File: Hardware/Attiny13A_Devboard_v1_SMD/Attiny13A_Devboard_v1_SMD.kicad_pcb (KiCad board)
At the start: 2 copper layers, 0 parts

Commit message: Attiny13A Dev Board SMD - Layout - Initial Placement done
Signed-off-by: alexanderjg85 <alexanderjg85@gmail.com>
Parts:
- added C1: 10 uF, Capacitor_SMD:C_1206_3216Metric_Pad1.33x1.80mm_HandSolder, F.Cu at (138.8, 64.2)
- added C2: 100 nF, Capacitor_SMD:C_1206_3216Metric_Pad1.33x1.80mm_HandSolder, F.Cu at (156.2, 80.5)
- added D1: SS14, Diode_SMD:D_SMA_Handsoldering, F.Cu at (130.5, 62.8)
- added D2: RED, LED_SMD:LED_1206_3216Metric_Pad1.42x1.75mm_HandSolder, F.Cu at (139.8, 79.2)
- added J1: Screw_Terminal_01x02, TerminalBlock_Phoenix:TerminalBlock_Phoenix_MKDS-1,5-2-5.08_1x02_P5.08mm_Horizontal, F.Cu at (128.6, 71.2)
- added J2: AVR-ISP-6, Connector_PinHeader_2.54mm:PinHeader_2x03_P2.54mm_Vertical, F.Cu at (156.2, 62.4)
- added J3: Conn_01x06_Pin, Connector_PinHeader_2.54mm:PinHeader_1x06_P2.54mm_Vertical, F.Cu at (168.5, 79.3)
- added R1: 470, Resistor_SMD:R_1206_3216Metric_Pad1.30x1.75mm_HandSolder, F.Cu at (146.2, 79.2)
- added R2: 10k, Resistor_SMD:R_1206_3216Metric_Pad1.30x1.75mm_HandSolder, F.Cu at (148.5, 64.2)
- added SW1: SW_Push, Button_Switch_SMD:SW_SPST_PTS647_Sx38, F.Cu at (143.5, 71.2)
- added TP1: TP_5V, TestPoint:TestPoint_Pad_D1.5mm, F.Cu at (125.2, 66.5)
- added TP2: TP_AVRLED, TestPoint:TestPoint_Pad_D1.5mm, F.Cu at (149.2, 75.8)
- added TP3: TP_VCC, TestPoint:TestPoint_Pad_D1.5mm, F.Cu at (143.8, 62.5)
- added TP4: TP_AVR_RST, TestPoint:TestPoint_Pad_D1.5mm, F.Cu at (150.2, 69.2)
- added TP5: TP_AVR_PB3, TestPoint:TestPoint_Pad_D1.5mm, F.Cu at (162.5, 69.5)
- added TP6: TP_AVR_SCK, TestPoint:TestPoint_Pad_D1.5mm, F.Cu at (152.8, 65.0)
- added TP7: TP_AVR_MISO, TestPoint:TestPoint_Pad_D1.5mm, F.Cu at (162.8, 74.2)
- added TP8: TP_AVR_MOSI, TestPoint:TestPoint_Pad_D1.5mm, F.Cu at (162.8, 77.8)
- added TP9: TP_GND, TestPoint:TestPoint_Pad_D1.5mm, F.Cu at (128.8, 81.5)
- added U1: ATtiny13A-SS, Package_SO:SOIC-8_3.9x4.9mm_P1.27mm, F.Cu at (156.0, 75.0)
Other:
- board outline added: 48 x 24 mm

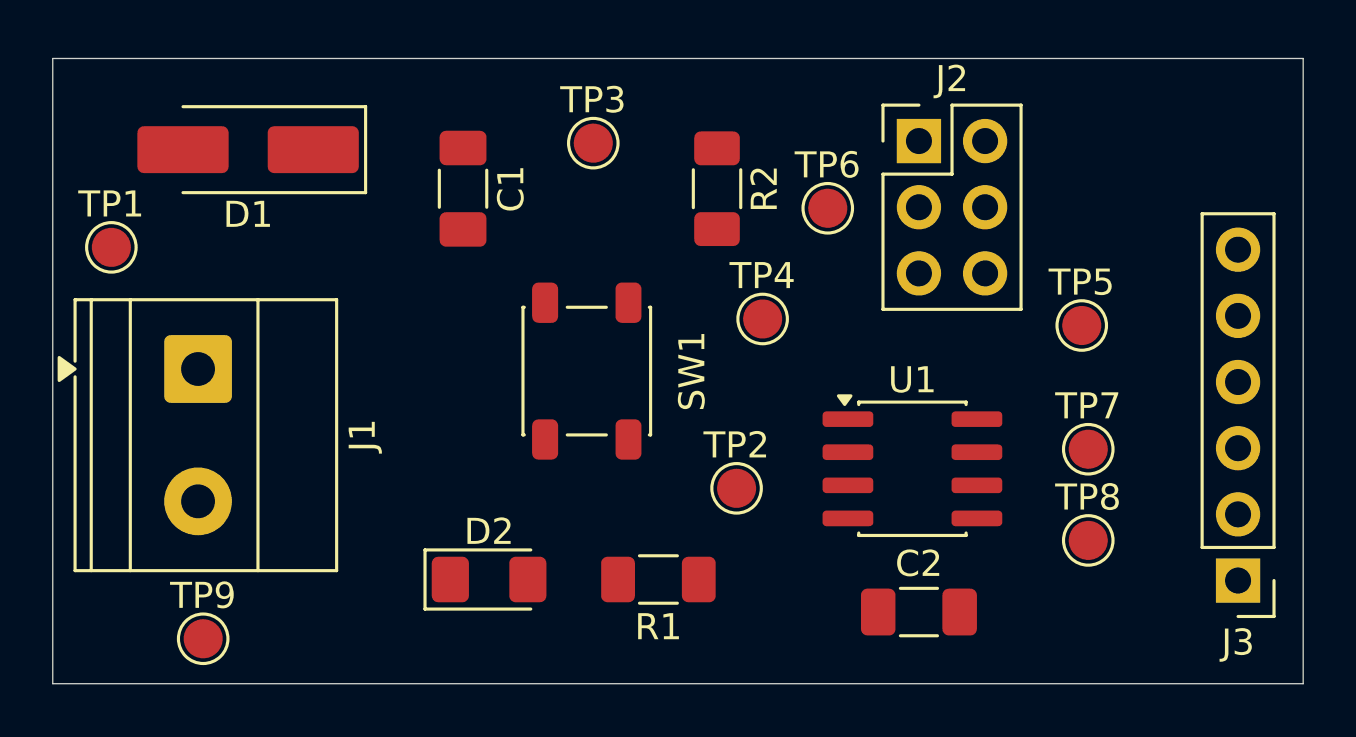
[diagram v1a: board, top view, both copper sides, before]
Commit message: Attiny13A Dev Board SMD - Layout - Initial Routing done
Signed-off-by: alexanderjg85 <alexanderjg85@gmail.com>
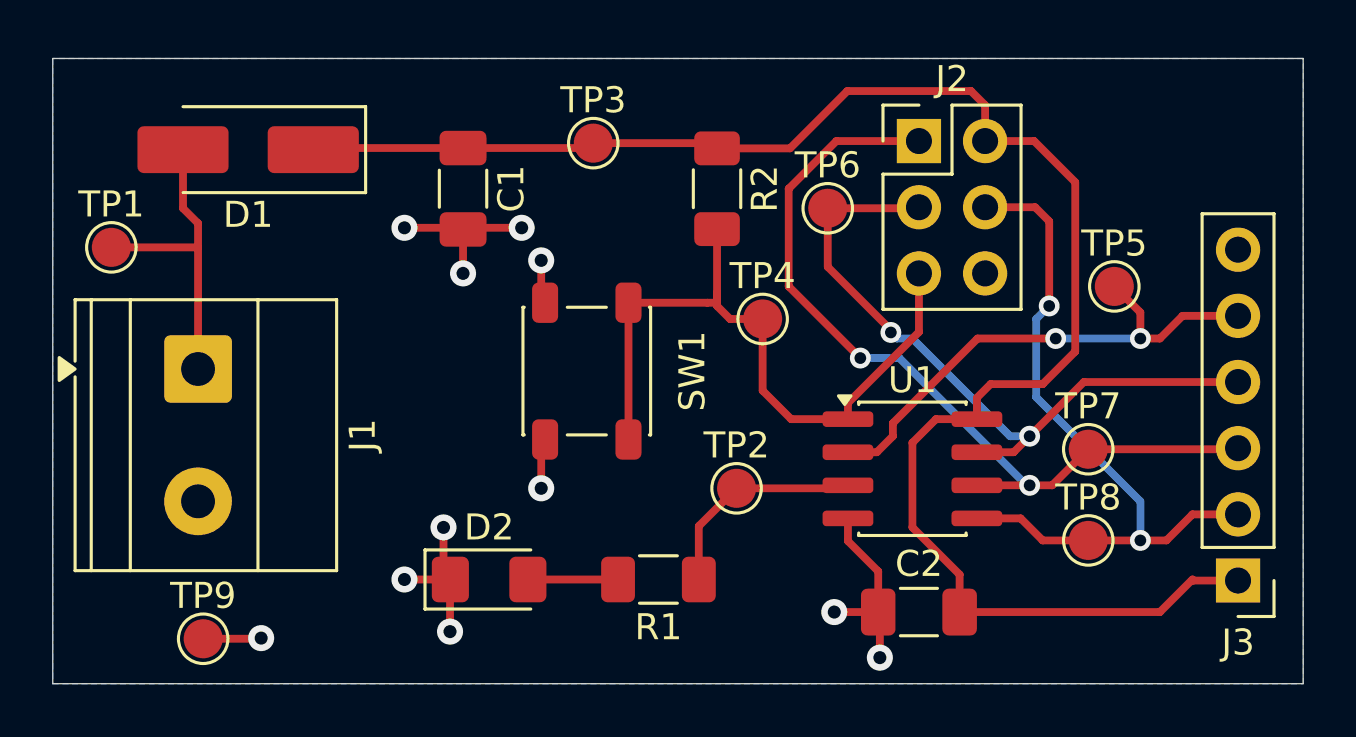
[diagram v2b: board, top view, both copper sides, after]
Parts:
- moved TP5 1.95 mm to (163.8, 68.0)
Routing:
- net VCC: track 0.00 -> 65.8 mm
- net AVR_MISO: track 0.00 -> 32.5 mm, vias 0 -> 2
- net AVR_MOSI: track 0.00 -> 27.6 mm, vias 0 -> 2
- net AVR_SCK: track 0.00 -> 27.4 mm, vias 0 -> 2
- net AVR_RST: track 0.00 -> 27.1 mm
- net GND: track 0.00 -> 25.5 mm, vias 0 -> 11
- net AVR_PB3: track 0.00 -> 19.9 mm, vias 0 -> 2
- net +5V: track 0.00 -> 12.0 mm
- net AVR_LED: track 0.00 -> 8.42 mm
- net Net-(D2-A): track 0.00 -> 3.46 mm
- added copper zone on B.Cu, net GND

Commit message: Attiny13A Dev Board SMD - Layout - Optimized Silk Screen
Signed-off-by: alexanderjg85 <alexanderjg85@gmail.com>
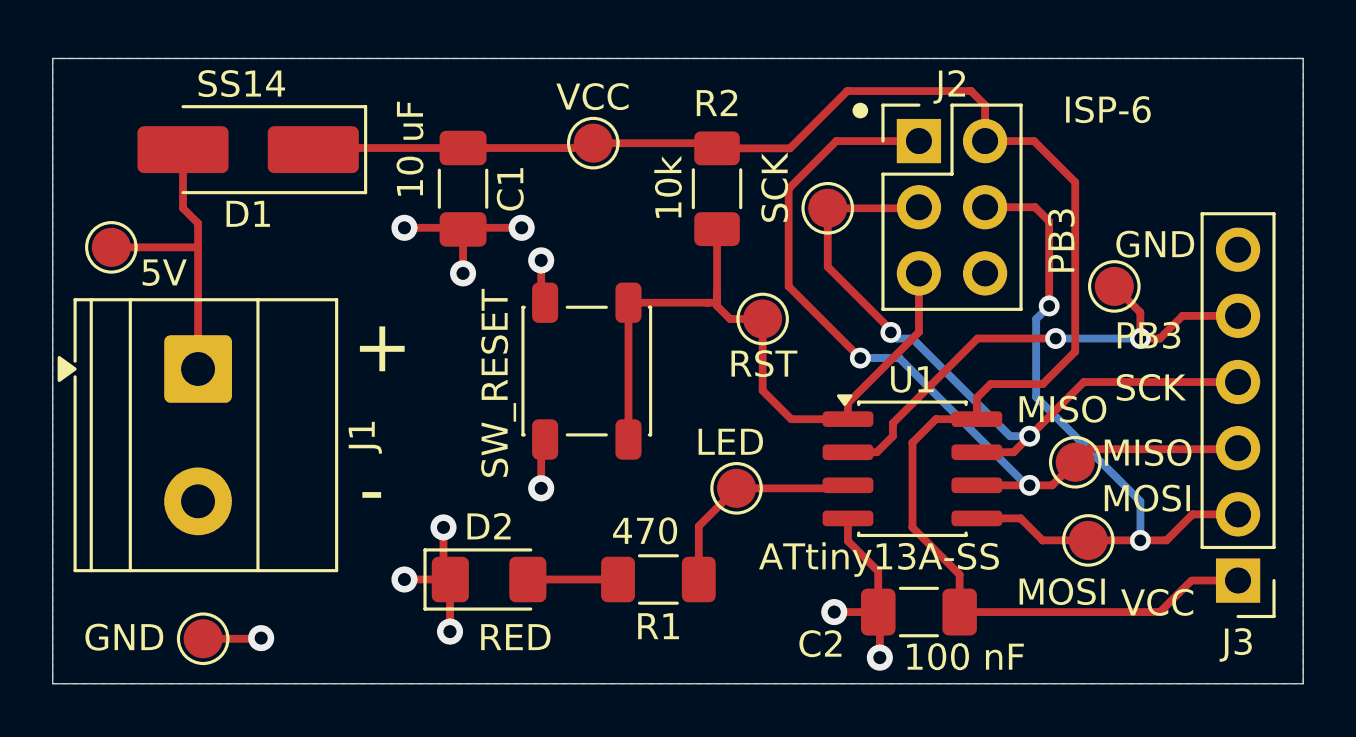
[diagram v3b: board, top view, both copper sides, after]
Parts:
- J2: value AVR-ISP-6 -> ISP-6
- SW1: value SW_Push -> SW_RESET
- TP1: value TP_5V -> 5V
- TP2: value TP_AVRLED -> LED
- TP3: value TP_VCC -> VCC
- TP4: value TP_AVR_RST -> RST
- TP5: value TP_AVR_PB3 -> PB3
- TP6: value TP_AVR_SCK -> SCK
- TP7: value TP_AVR_MISO -> MISO
- TP8: value TP_AVR_MOSI -> MOSI
- TP9: value TP_GND -> GND
- moved TP7 0.71 mm to (162.2, 74.8)
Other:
- board text added: "+"
- board text added: "-"
- board text added: "Alexander Jaeger 2026"
- board text added: "Attiny13A Devboard V1 SMD"
- board text added: "GND"
- board text added: "MISO"
- board text added: "MOSI"
- board text added: "PB3"
- board text added: "SCK"
- board text added: "VCC"
